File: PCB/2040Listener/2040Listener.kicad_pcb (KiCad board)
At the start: 2 copper layers, 73 x 34.5 mm, 34 parts, among them J1 CONN4_292303_SOCKET, J2 USB-AP-S-RA-PLUG, SW1 PTS815 SJM 250 SMTR LFS, SW2 PTS815 SJM 250 SMTR LFS, U1 RP2040, U2 NCP1117-3.3_SOT223, U4 BY25Q16AWTIG(R), Y1 ABM8-272-T3

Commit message: attempt to fix usb connector
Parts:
- moved J2 0.12 mm to (104.2, 63.9)
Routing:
- net VBUS: track 98.5 -> 114.8 mm
- net +3V3: track 75.2 -> 69.2 mm, vias 1 -> 0
- net GND: track 65.3 -> 68.3 mm, vias 13 -> 14
- net /USB_D-: track 31.7 -> 32.3 mm, vias 1 -> 2
- net /USB_D+: track 32.2 -> 32.5 mm, vias 1 -> 0

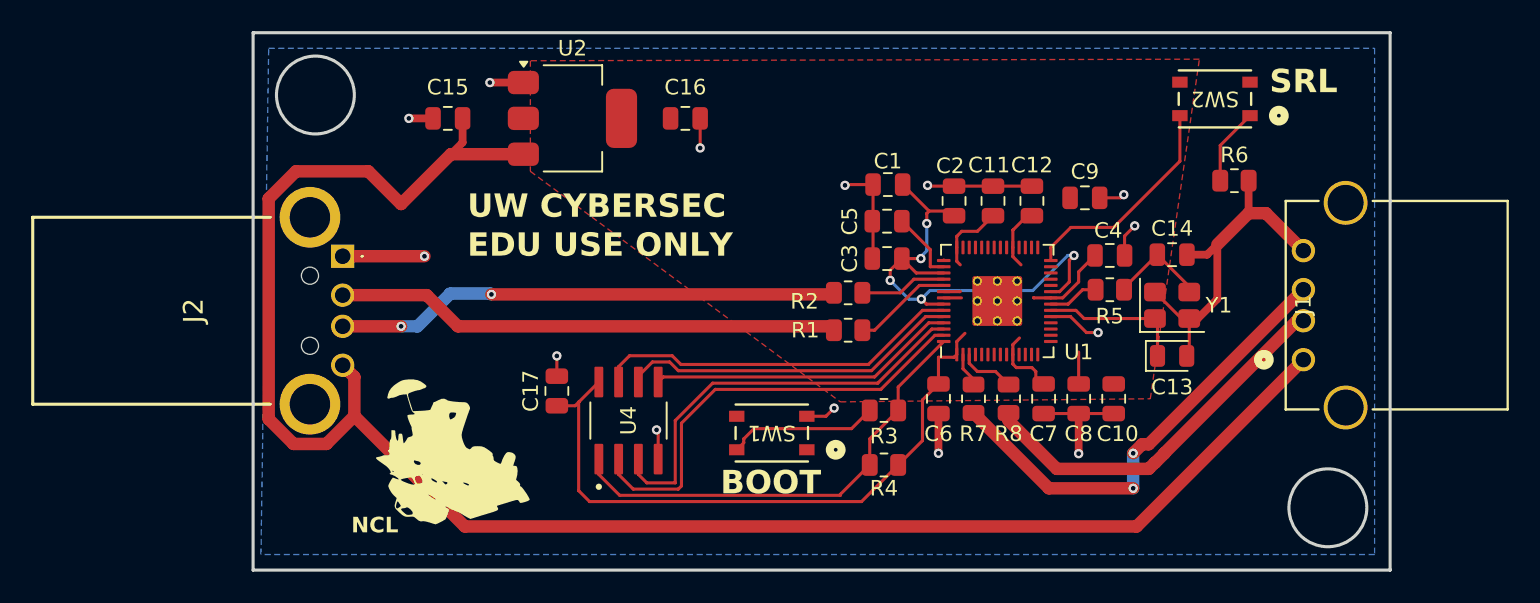
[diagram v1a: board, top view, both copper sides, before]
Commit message: flip usb plugs
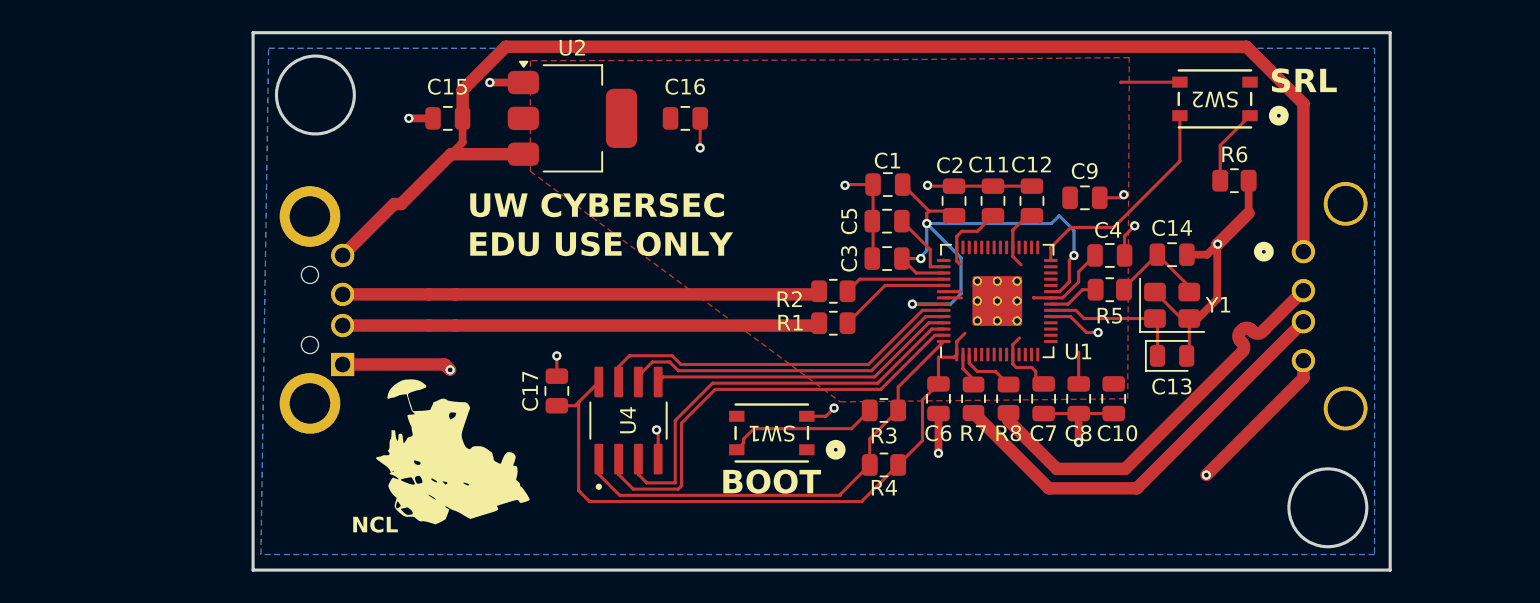
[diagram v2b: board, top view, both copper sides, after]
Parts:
- J1, J2: moved to B.Cu
- moved J2 6.95 mm to (104.2, 70.8), turned to 90 degrees
- moved J1 6.94 mm to (165.9, 63.6), turned to -90 degrees
- moved R1 1.05 mm to (135.8, 68.2)
- moved R2 0.96 mm to (135.8, 66.1)
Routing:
- net VBUS: track 114.8 -> 84.9 mm
- net GND: track 68.3 -> 74.7 mm, vias 14 -> 16
- net +1V1: track 31.6 -> 37.4 mm, vias 5 -> 4
- net +3V3: track 69.2 -> 73.1 mm
- net /GPIO0: track 29.8 -> 27.6 mm, vias 2 -> 0
- net /GPIO1: track 24.7 -> 26.7 mm
- net /USB_D+: track 32.5 -> 30.6 mm
- net /USB_D-: track 32.3 -> 30.7 mm, vias 2 -> 0
- net Net-(U1-USB_DM): track 5.59 -> 6.50 mm
- net Net-(U1-USB_DP): track 6.42 -> 7.19 mm

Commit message: pcb works!
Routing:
- net +3V3: track 73.1 -> 142.2 mm
- net /GPIO1: track 26.7 -> 25.4 mm
- removed copper zone on F.Cu, net +3V3

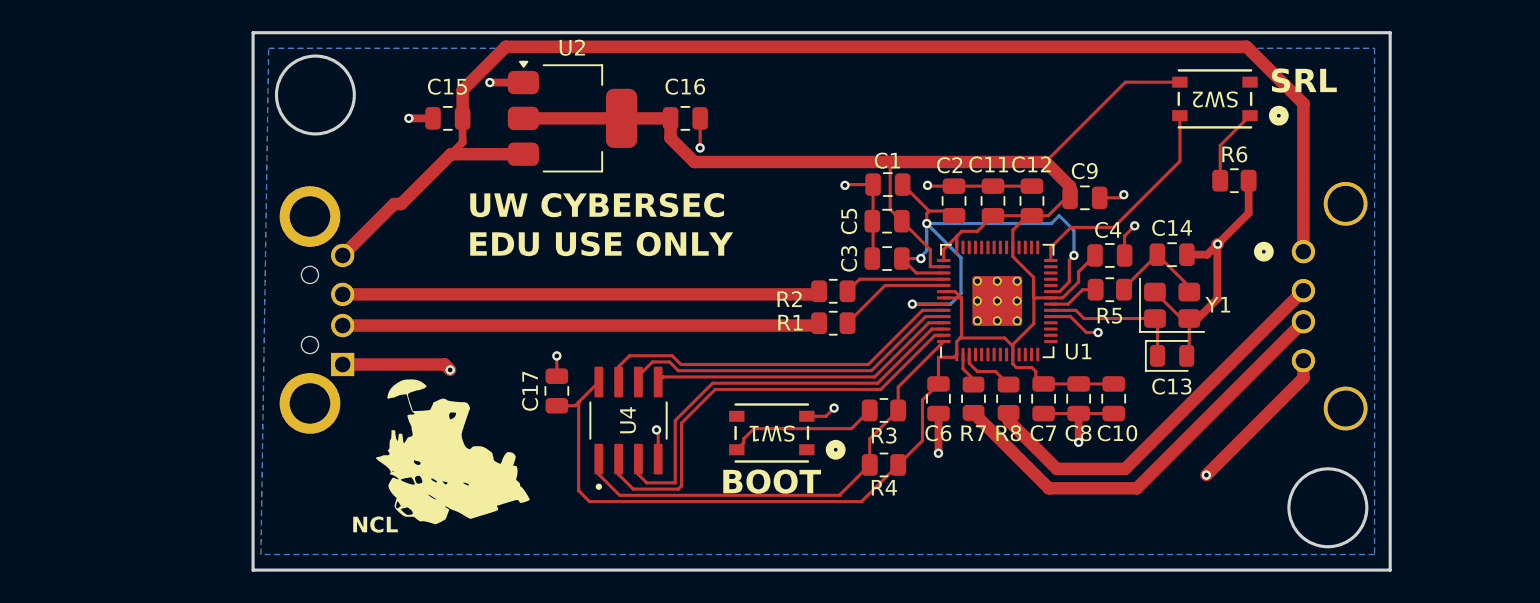
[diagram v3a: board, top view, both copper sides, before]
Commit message: update pcb spacing
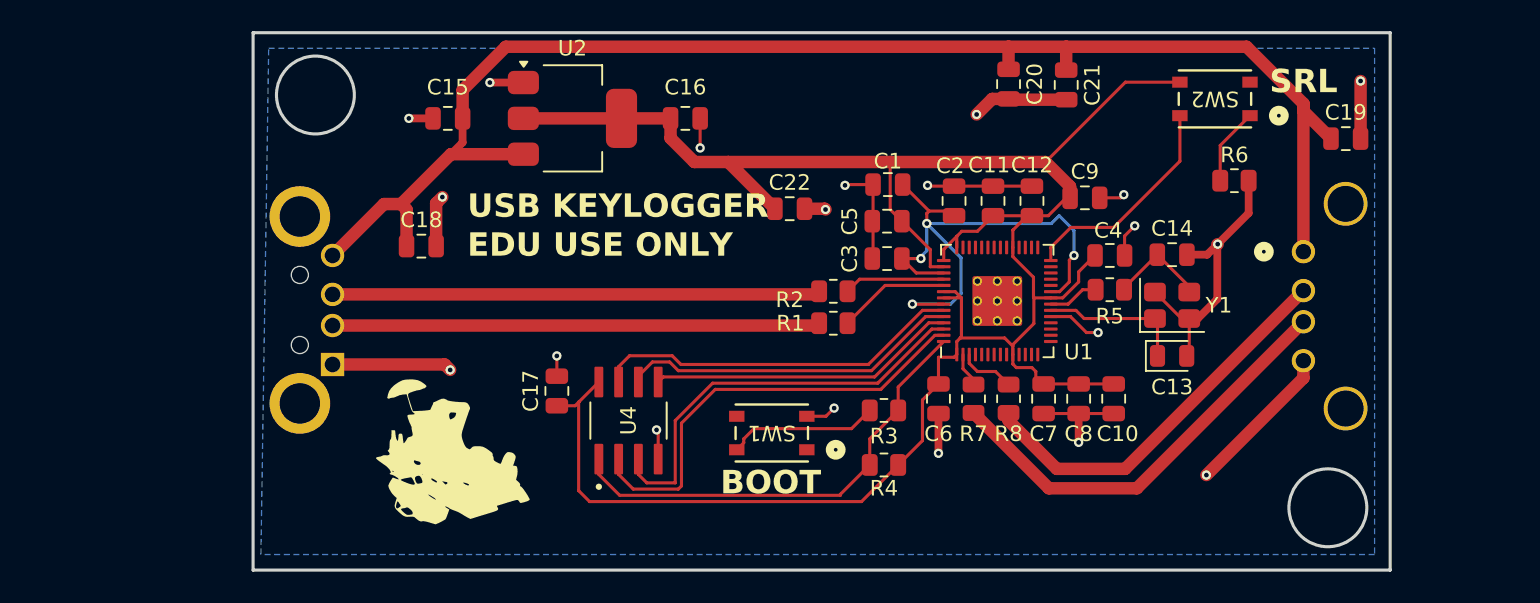
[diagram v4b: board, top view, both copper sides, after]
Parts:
- added C18: 10u, Capacitor_SMD:C_0805_2012Metric, F.Cu at (109.3, 63.2)
- added C19: 10u, Capacitor_SMD:C_0805_2012Metric, F.Cu at (168.7, 56.3)
- added C20: 10u, Capacitor_SMD:C_0805_2012Metric, F.Cu at (147.0, 52.8)
- added C21: 10u, Capacitor_SMD:C_0805_2012Metric, F.Cu at (150.7, 52.9)
- added C22: 10u, Capacitor_SMD:C_0805_2012Metric, F.Cu at (132.9, 60.8)
- moved J2 0.65 mm to (103.6, 70.8)
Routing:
- net GND: track 74.8 -> 89.3 mm, vias 16 -> 20
- net VBUS: track 84.9 -> 94.3 mm
- net +3V3: track 142.2 -> 146.4 mm
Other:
- board text added: "USB KEYLOGGER"
- board text removed: "NCL"
- board text removed: "UW CYBERSEC"
